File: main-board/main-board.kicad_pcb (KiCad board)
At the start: 2 copper layers, 101 x 101 mm, 57 parts, among them J1 C10418, J2 FH12-24S-0.5SH(55), J3 TF-01A, Q1 Q_NPN_BCE, Q2 Q_NPN_BCE, SW1 SW_DIP_x01, U1 ESP-32s, U2 HT7333-A, U3 CH340E, U4 DW06D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

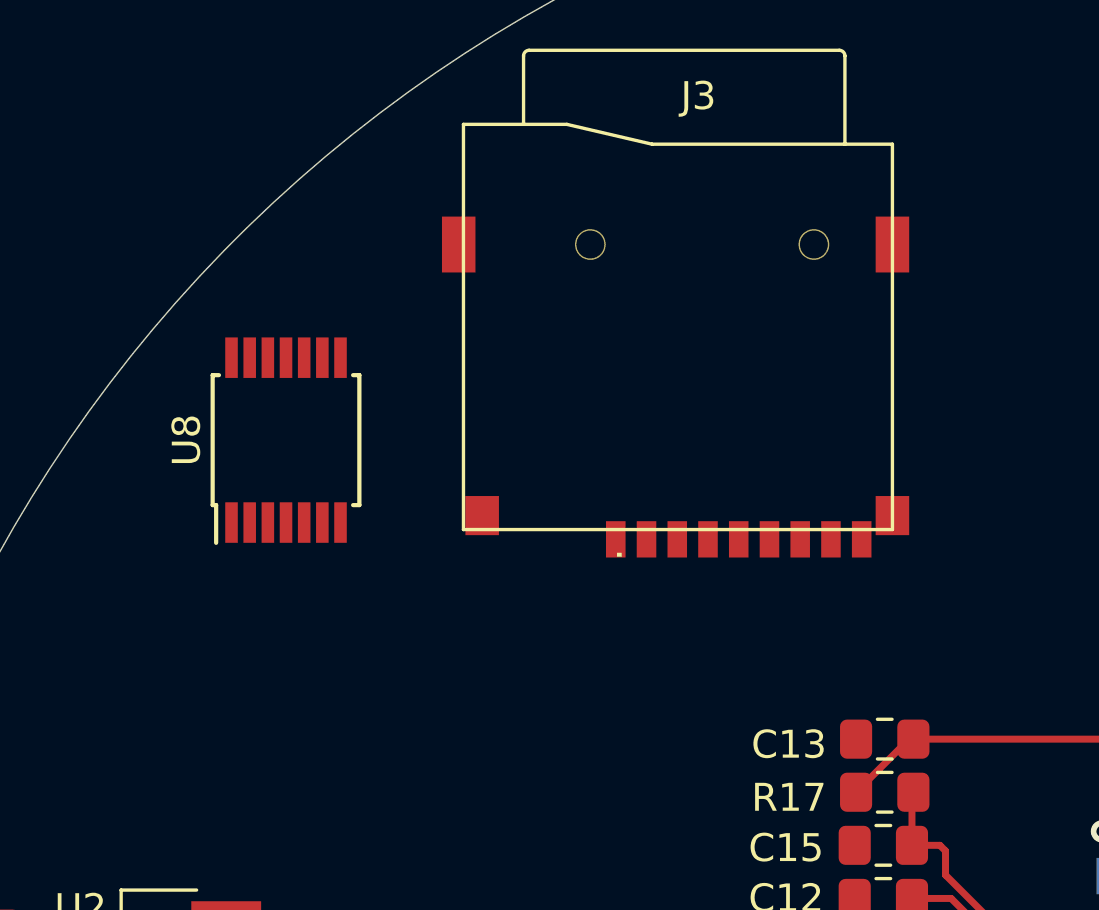
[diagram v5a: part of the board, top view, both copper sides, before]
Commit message: SD passive and wires
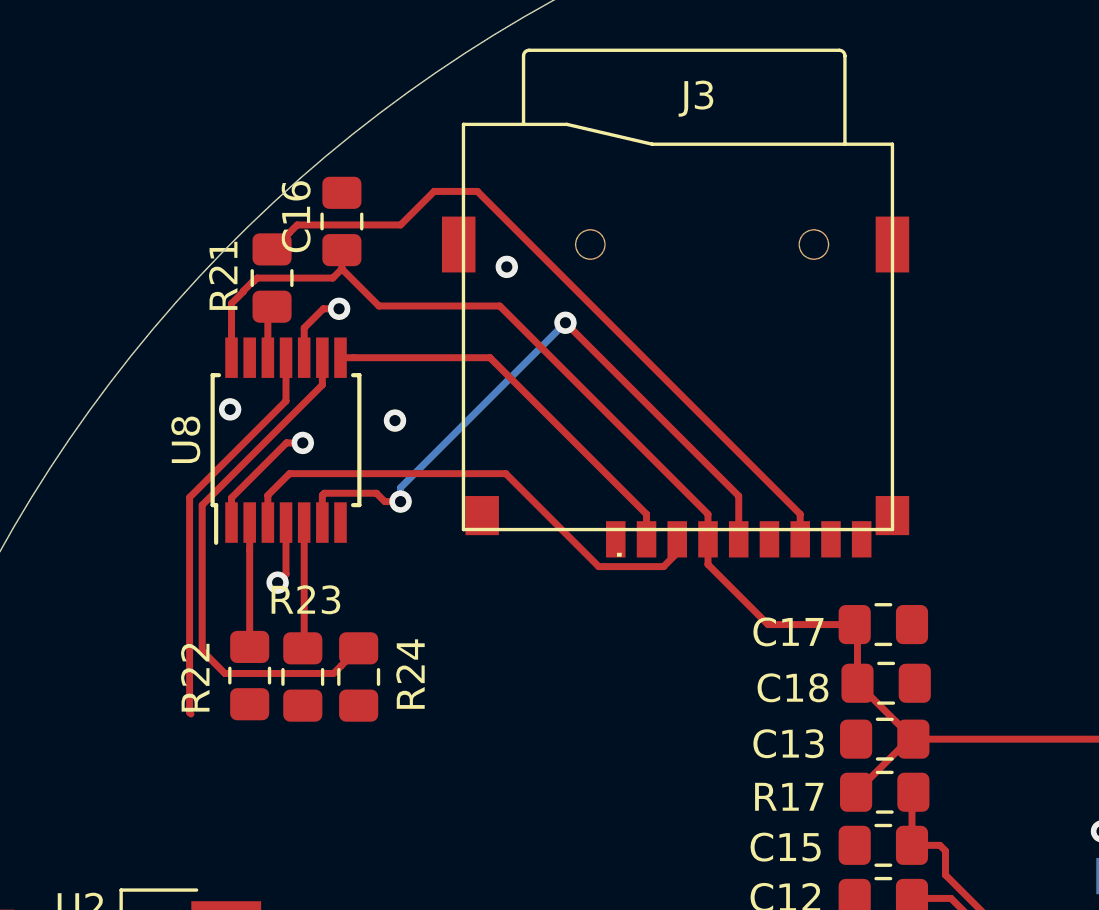
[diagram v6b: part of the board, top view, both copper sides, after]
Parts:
- added C16: 10uF, Capacitor_SMD:C_0805_2012Metric_Pad1.15x1.40mm_HandSolder, F.Cu at (113.1, 53.7)
- added C17: 0.1uF, Capacitor_SMD:C_0805_2012Metric_Pad1.15x1.40mm_HandSolder, F.Cu at (132.5, 68.1)
- added C18: 0.1uF, Capacitor_SMD:C_0805_2012Metric_Pad1.15x1.40mm_HandSolder, F.Cu at (132.6, 70.2)
- added R21: 3k3, Resistor_SMD:R_0805_2012Metric_Pad1.15x1.40mm_HandSolder, F.Cu at (110.6, 55.7)
- added R22: 3k3, Resistor_SMD:R_0805_2012Metric_Pad1.15x1.40mm_HandSolder, F.Cu at (109.8, 69.9)
- added R23: 3k3, Resistor_SMD:R_0805_2012Metric_Pad1.15x1.40mm_HandSolder, F.Cu at (111.7, 70.0)
- added R24: 3k3, Resistor_SMD:R_0805_2012Metric_Pad1.15x1.40mm_HandSolder, F.Cu at (113.7, 70.0)
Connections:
- net Net-(U8-Pad11) renamed /SD_MISO
- J3 pad 10: Net-(J3-Pad10) -> GND
- J3 pad 11: Net-(J3-Pad11) -> GND
- J3 pad 12: Net-(J3-Pad12) -> GND
- J3 pad 13: Net-(J3-Pad13) -> GND
- J3 pad 2: Net-(J3-Pad2) -> /SD_D3
- J3 pad 3: Net-(J3-Pad3) -> /SD_CMD
- J3 pad 4: Net-(J3-Pad4) -> +3V3
- J3 pad 5: Net-(J3-Pad5) -> /SD_CLK
- J3 pad 6: Net-(J3-Pad6) -> GND
- U8 pad 1: Net-(U8-Pad1) -> GND
- U8 pad 10: Net-(U8-Pad10) -> GND
- U8 pad 12: Net-(U8-Pad12) -> /SD_D0
- U8 pad 13: Net-(U8-Pad13) -> GND
- U8 pad 14: Net-(U8-Pad14) -> +3V3
- U8 pad 3: Net-(U8-Pad3) -> /SD_CMD
- U8 pad 4: Net-(U8-Pad4) -> GND
- U8 pad 6: Net-(U8-Pad6) -> /SD_CLK
- U8 pad 7: Net-(U8-Pad7) -> GND
- U8 pad 8: Net-(U8-Pad8) -> /SD_D3
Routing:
- net +3V3: track 186.8 -> 223.5 mm
- net Net-(J3-Pad7): track 0.00 -> 25.5 mm
- net /SD_CLK: track 0.00 -> 23.1 mm, vias 0 -> 2
- net Net-(R24-Pad1): track 0.00 -> 18.6 mm
- net /SD_CMD: track 0.00 -> 18.0 mm
- net /SD_MISO: track 0.00 -> 14.2 mm
- net /SD_D3: track 0.00 -> 14.2 mm
- net GND: track 12.6 -> 21.7 mm, vias 57 -> 63
- net Net-(R23-Pad2): track 0.00 -> 4.52 mm
- net Net-(R22-Pad2): track 0.00 -> 4.45 mm
- net /SD_D0: track 0.00 -> 1.91 mm

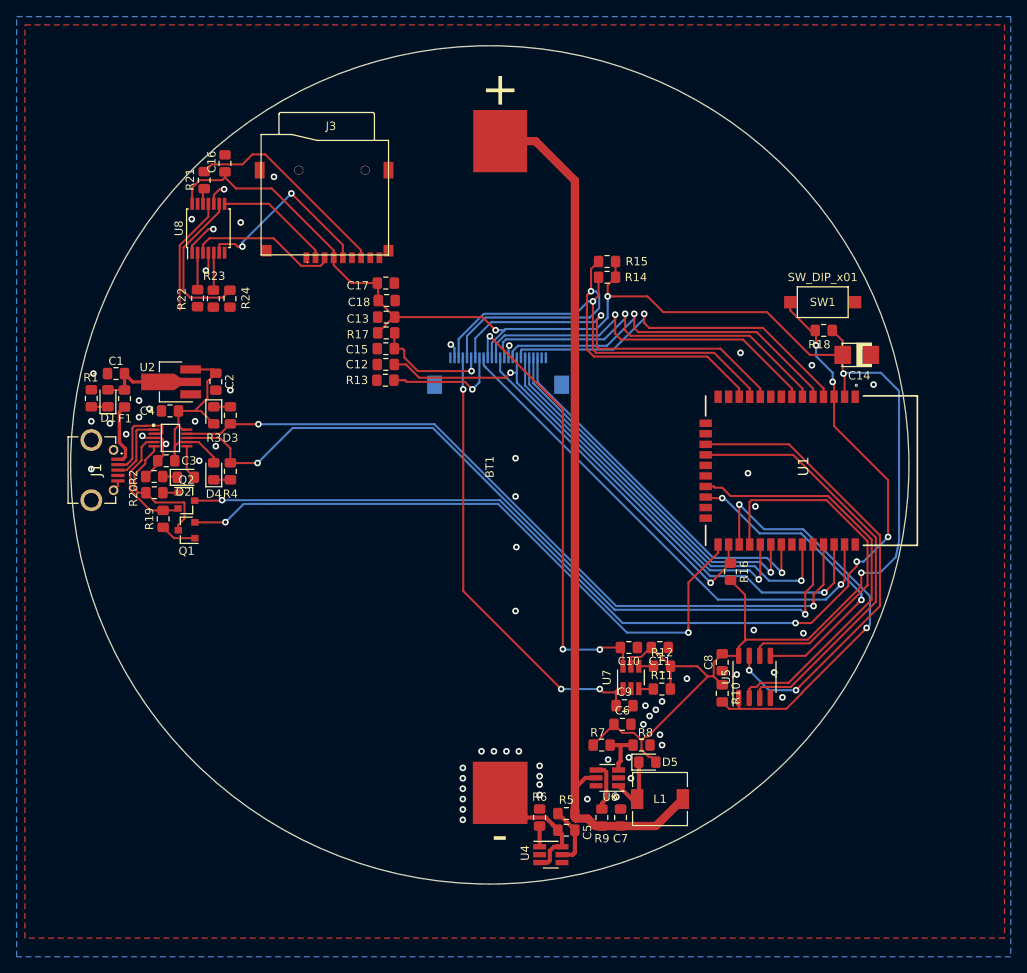
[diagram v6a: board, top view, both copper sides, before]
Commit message: LED and few connection
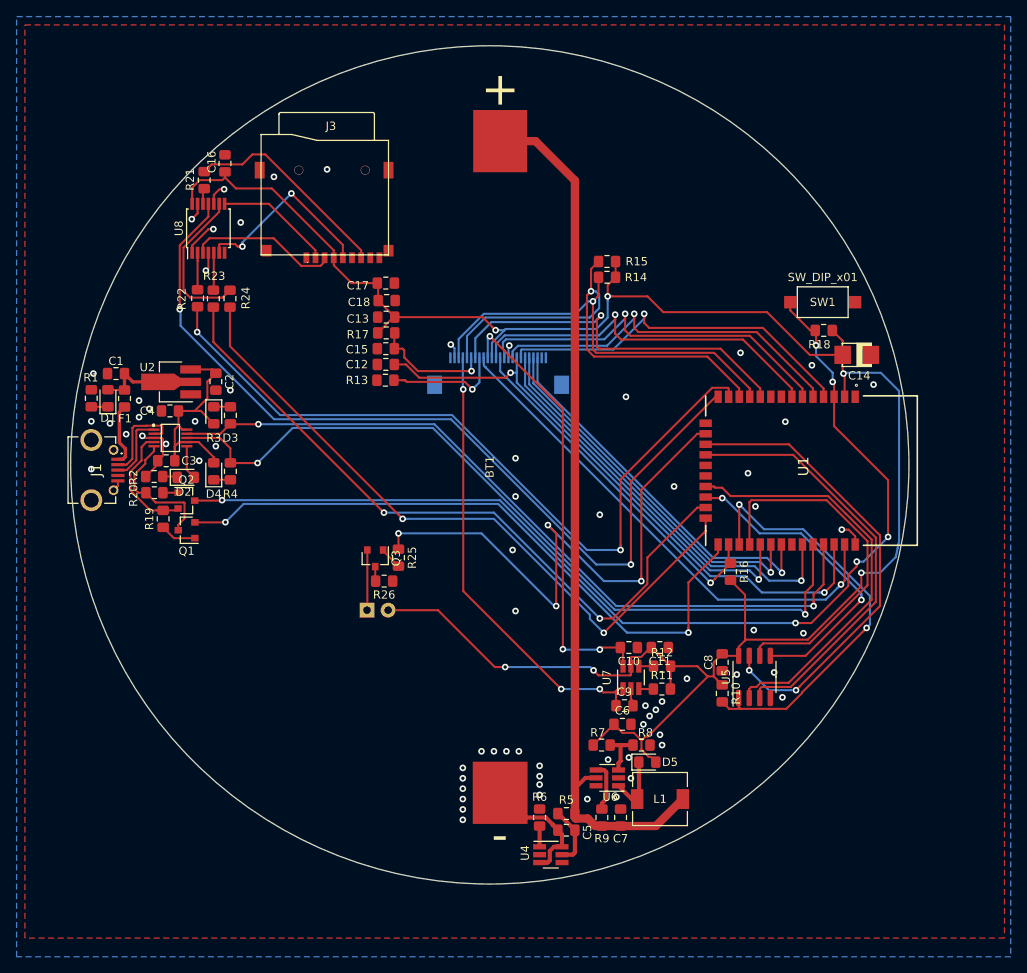
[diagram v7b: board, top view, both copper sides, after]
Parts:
- added D6: LED, LED_THT:LED_D3.0mm, B.Cu at (130.2, 107.5)
- added Q3: Q_NPN_BCE, Package_TO_SOT_SMD:SOT-23, F.Cu at (131.2, 101.2)
- added R25: 1k, Resistor_SMD:R_0805_2012Metric_Pad1.15x1.40mm_HandSolder, F.Cu at (134.0, 101.2)
- added R26: 1k, Resistor_SMD:R_0805_2012Metric_Pad1.15x1.40mm_HandSolder, F.Cu at (132.3, 104.0)
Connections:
- J2 pad 26: Net-(J2-Pad26) -> GND
- U1 pad 13: Net-(U1-Pad13) -> /SD_MOSI
- U1 pad 14: Net-(U1-Pad14) -> /SD_MISO
- U1 pad 15: Net-(U1-Pad15) -> GND
- U1 pad 16: Net-(U1-Pad16) -> /IO13
- U1 pad 23: Net-(U1-Pad23) -> /SD_SCK
- U1 pad 24: Net-(U1-Pad24) -> /SD_CS
- U1 pad 38: Net-(U1-Pad38) -> GND
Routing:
- net /SD_MISO: track 14.2 -> 107.7 mm, vias 0 -> 2
- net /SD_MOSI: track 0.00 -> 92.1 mm, vias 0 -> 2
- net /SD_SCK: track 0.00 -> 84.7 mm, vias 0 -> 2
- net /SD_CS: track 0.00 -> 83.3 mm, vias 0 -> 2
- net /IO13: track 0.00 -> 70.3 mm, vias 0 -> 4
- net +3V3: track 223.5 -> 257.1 mm, vias 4 -> 6
- net Net-(D6-Pad1): track 0.00 -> 7.27 mm
- net GND: track 21.7 -> 29.0 mm, vias 63 -> 69
- net Net-(Q3-Pad1): track 0.00 -> 2.77 mm
- net Net-(Q3-Pad3): track 0.00 -> 1.77 mm

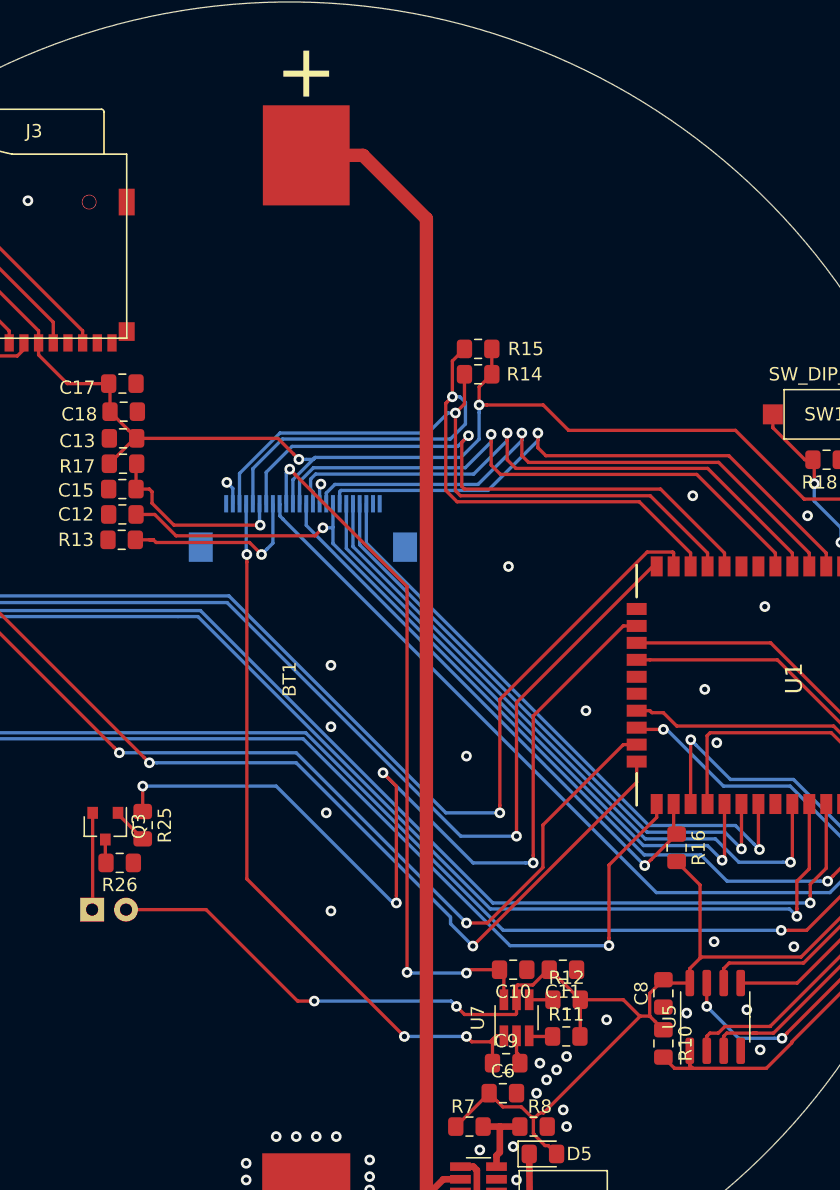
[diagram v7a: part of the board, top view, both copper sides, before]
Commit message: LED SMD
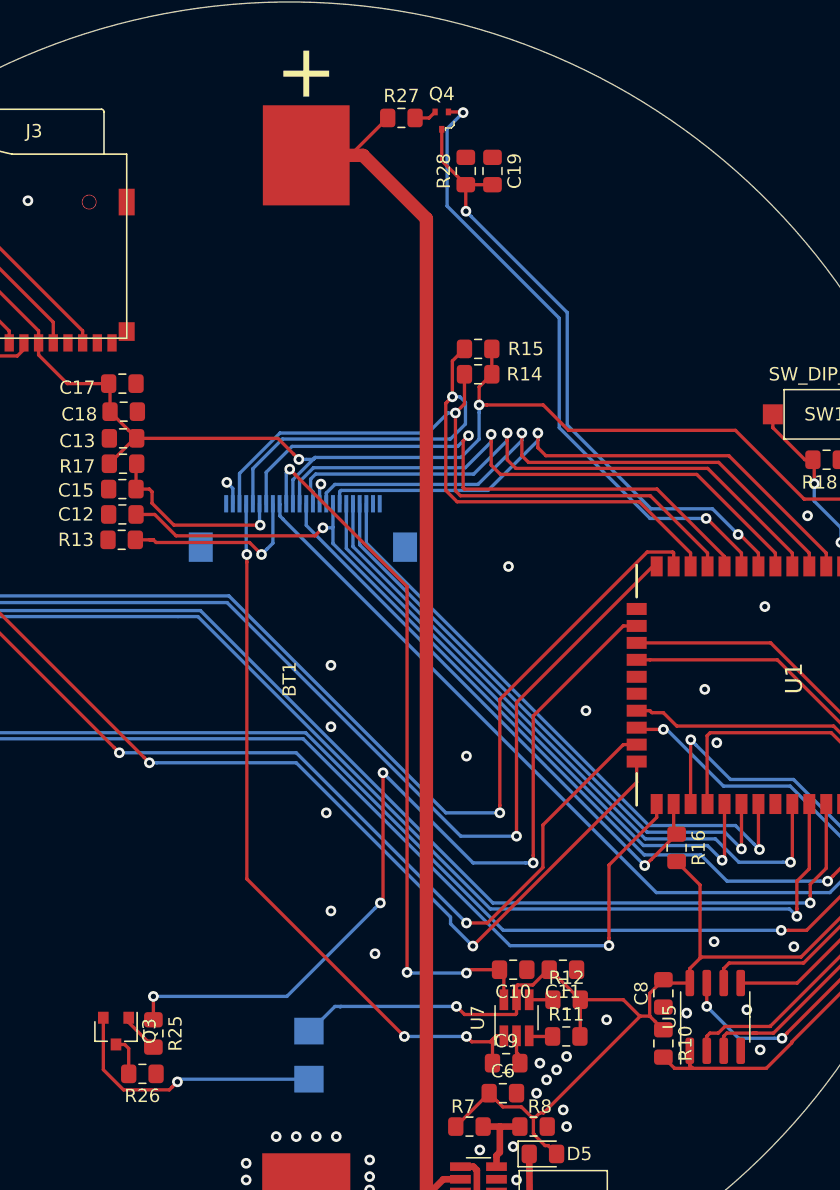
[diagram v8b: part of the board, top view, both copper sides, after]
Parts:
- added C19: 1uF, Capacitor_SMD:C_0805_2012Metric_Pad1.15x1.40mm_HandSolder, F.Cu at (160.2, 52.2)
- added Q4: DMG1012T, water-lib:SOT-523, F.Cu at (156.4, 48.4)
- added R27: 27k, Resistor_SMD:R_0805_2012Metric_Pad1.15x1.40mm_HandSolder, F.Cu at (153.4, 48.2)
- added R28: 10k, Resistor_SMD:R_0805_2012Metric_Pad1.15x1.40mm_HandSolder, F.Cu at (158.2, 52.2)
- D6: value LED -> HQ67-2100IRC; footprint LED_THT:LED_D3.0mm -> water-lib:HQ67-2100IRC
- moved D6 19.5 mm to (146.4, 118.4), turned to 90 degrees
- moved R26 15.9 mm to (134.0, 119.8)
- moved R25 15.6 mm to (134.8, 116.8)
- moved Q3 15.4 mm to (132.0, 116.6)
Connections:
- U1 pad 8: Net-(U1-Pad8) -> /IO32
- U1 pad 9: Net-(U1-Pad9) -> /BAT_ST
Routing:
- net /IO32: track 0.00 -> 47.3 mm, vias 0 -> 2
- net /BAT_ST: track 0.00 -> 47.2 mm, vias 0 -> 2
- net +3V3: track 257.1 -> 241.2 mm, vias 6 -> 5
- net Net-(D6-Pad1): track 7.27 -> 20.2 mm, vias 0 -> 1
- net /VBAT: track 108.6 -> 115.8 mm
- net /IO13: track 70.3 -> 67.1 mm
- net Net-(Q4-Pad2): track 0.00 -> 1.69 mm
- net Net-(Q3-Pad3): track 1.77 -> 2.97 mm
